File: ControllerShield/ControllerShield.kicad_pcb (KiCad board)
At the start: 2 copper layers, 68.6 x 53.5 mm, 30 parts, among them J1 Power, J2 Digital/PWM, J3 Analog, J4 Digital/PWM, J5 Conn_02x05_Odd_Even, J6 Debug Point, SW1 Small Switch TH, U1 COM-09032, U2 LIS3DHTR, U3 TLV75533PDBV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

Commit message: Close #13
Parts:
- moved D2 5.05 mm to (128.1, 91.7)
- moved D1 2.90 mm to (128.0, 134.7)
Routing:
- net Net-(D2-A): track 3.83 -> 8.00 mm, vias 0 -> 1
- net Net-(D1-A): track 30.9 -> 33.7 mm
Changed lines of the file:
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@@
   )
   (footprint "LED_THT:LED_D5.0mm" (layer "F.Cu")
-    (at 128 131.75)
+    (at 128.025 134.65)
     (descr "LED, diameter 5.0mm, 2 pins, http://cdn-reichelt.de/documents/datenblatt/A500/LL-504BC2E-009.pdf")
     (tags "LED diameter 5.0mm 2 pins")
@@
   )
   (footprint "LED_THT:LED_D5.0mm" (layer "F.Cu")
-    (at 128 96.75)
+    (at 128.075 91.7)
     (descr "LED, diameter 5.0mm, 2 pins, http://cdn-reichelt.de/documents/datenblatt/A500/LL-504BC2E-009.pdf")
     (tags "LED diameter 5.0mm 2 pins")
@@
     (property "ki_keywords" "LED diode")
     (attr through_hole)
-    (fp_text reference "D2" (at 1.27 -3.96) (layer "F.SilkS")
+    (fp_text reference "D2" (at -3.175 -0.5) (layer "F.SilkS")
         (effects (font (size 1 1) (thickness 0.15)))
     )
@@
   (segment (start 134 102.325) (end 134 103.75) (width 0.18) (layer "F.Cu") (net 5))
   (via (at 134 103.75) (size 0.5) (drill 0.3) (layers "F.Cu" "B.Cu") (net 5))
-  (segment (start 134 128.29) (end 130.54 131.75) (width 0.18) (layer "B.Cu") (net 5))
-  (segment (start 134 103.75) (end 134 128.29) (width 0.18) (layer "B.Cu") (net 5))
-  (segment (start 134 97.65) (end 133.1 96.75) (width 0.18) (layer "F.Cu") (net 6))
-  (segment (start 133.1 96.75) (end 130.54 96.75) (width 0.18) (layer "F.Cu") (net 6))
+  (segment (start 134 131.215) (end 130.565 134.65) (width 0.18) (layer "B.Cu") (net 5))
+  (segment (start 134 103.75) (end 134 131.215) (width 0.18) (layer "B.Cu") (net 5))
+  (segment (start 134 97.65) (end 132.9 97.65) (width 0.2) (layer "F.Cu") (net 6))
+  (segment (start 132.9 97.65) (end 132.6 97.35) (width 0.2) (layer "F.Cu") (net 6))
+  (via (at 132.6 97.35) (size 0.5) (drill 0.3) (layers "F.Cu" "B.Cu") (net 6))
+  (segment (start 132.6 97.35) (end 132.6 93.685) (width 0.2) (layer "B.Cu") (net 6))
+  (segment (start 132.6 93.685) (end 130.615 91.7) (width 0.2) (layer "B.Cu") (net 6))
   (segment (start 136.525 110.988) (end 136.6 111.063) (width 0.18) (layer "F.Cu") (net 10))
   (segment (start 136.525 109.75) (end 136.525 110.988) (width 0.18) (layer "F.Cu") (net 10))
@@
   (segment (start 140.746 96.504) (end 140.746 90.395) (width 0.127) (layer "B.Cu") (net 10))
   (segment (start 127.21 117.54) (end 124.71 117.54) (width 1.27) (layer "F.Cu") (net 11))
-  (segment (start 150.906 90.395) (end 148.301 93) (width 0.18) (layer "F.Cu") (net 12))
-  (segment (start 148.301 93) (end 124.25 93) (width 0.18) (layer "F.Cu") (net 12))
+  (segment (start 147.951 93.35) (end 124.6 93.35) (width 0.18) (layer "F.Cu") (net 12))
+  (segment (start 124.6 93.35) (end 124.25 93) (width 0.18) (layer "F.Cu") (net 12))
+  (segment (start 150.906 90.395) (end 147.951 93.35) (width 0.18) (layer "F.Cu") (net 12))
   (via (at 124.25 93) (size 0.5) (drill 0.3) (layers "F.Cu" "B.Cu") (net 12))
   (segment (start 124.25 112.04) (end 127.21 115) (width 0.18) (layer "B.Cu") (net 12))
   (segment (start 124.25 93) (end 124.25 112.04) (width 0.18) (layer "B.Cu") (net 12))
-  (segment (start 150.341 93.5) (end 125.5 93.5) (width 0.18) (layer "F.Cu") (net 17))
-  (segment (start 125.5 93.5) (end 125 94) (width 0.18) (layer "F.Cu") (net 17))
-  (segment (start 153.446 90.395) (end 150.341 93.5) (width 0.18) (layer "F.Cu") (net 17))
+  (segment (start 125.2 93.8) (end 125 94) (width 0.18) (layer "F.Cu") (net 17))
+  (segment (start 150.041 93.8) (end 125.2 93.8) (width 0.18) (layer "F.Cu") (net 17))
+  (segment (start 153.446 90.395) (end 150.041 93.8) (width 0.18) (layer "F.Cu") (net 17))
   (via (at 125 94) (size 0.5) (drill 0.3) (layers "F.Cu" "B.Cu") (net 17))
   (segment (start 125 111.862204) (end 125 94) (width 0.18) (layer "B.Cu") (net 17))
@@
   (segment (start 141.25 92.431) (end 143.286 90.395) (width 0.127) (layer "B.Cu") (net 28))
   (segment (start 140.75 100.75) (end 140.5 100.5) (width 0.18) (layer "B.Cu") (net 28))
-  (segment (start 158.526 90.395) (end 154.921 94) (width 0.18) (layer "F.Cu") (net 34))
-  (segment (start 126.25 94) (end 125.75 94.5) (width 0.18) (layer "F.Cu") (net 34))
-  (segment (start 154.921 94) (end 126.25 94) (width 0.18) (layer "F.Cu") (net 34))
+  (segment (start 126 94.25) (end 125.75 94.5) (width 0.18) (layer "F.Cu") (net 34))
+  (segment (start 154.671 94.25) (end 126 94.25) (width 0.18) (layer "F.Cu") (net 34))
+  (segment (start 158.526 90.395) (end 154.671 94.25) (width 0.18) (layer "F.Cu") (net 34))
   (via (at 125.75 94.5) (size 0.5) (drill 0.3) (layers "F.Cu" "B.Cu") (net 34))
   (segment (start 125.5 94.75) (end 125.5 110.49) (width 0.18) (layer "B.Cu") (net 34))
@@
   (segment (start 128.61 111.06) (end 129.75 109.92) (width 0.18) (layer "B.Cu") (net 34))
   (segment (start 126.07 111.06) (end 128.61 111.06) (width 0.18) (layer "B.Cu") (net 34))
-  (segment (start 127.0395 94.4605) (end 126.25 95.25) (width 0.18) (layer "F.Cu") (net 39))
-  (segment (start 157.0005 94.4605) (end 127.0395 94.4605) (width 0.18) (layer "F.Cu") (net 39))
-  (segment (start 161.066 90.395) (end 157.0005 94.4605) (width 0.18) (layer "F.Cu") (net 39))
+  (segment (start 161.066 90.395) (end 156.811 94.65) (width 0.18) (layer "F.Cu") (net 39))
+  (segment (start 126.85 94.65) (end 126.25 95.25) (width 0.18) (layer "F.Cu") (net 39))
+  (segment (start 156.811 94.65) (end 126.85 94.65) (width 0.18) (layer "F.Cu") (net 39))
   (via (at 126.25 95.25) (size 0.5) (drill 0.3) (layers "F.Cu" "B.Cu") (net 39))
   (segment (start 126.25 95.25) (end 126.25 108.75) (width 0.18) (layer "B.Cu") (net 39))

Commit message: update qr code and legend
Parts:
- removed the G*** at (140.2, 125.8)
- added G***: LOGO, QRCodes:v0.9, F.Cu at (137.8, 125.0)
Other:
- board text added: "Maze Controller V0.9 Copyright 2023 Tad Truex Dartmouth College"

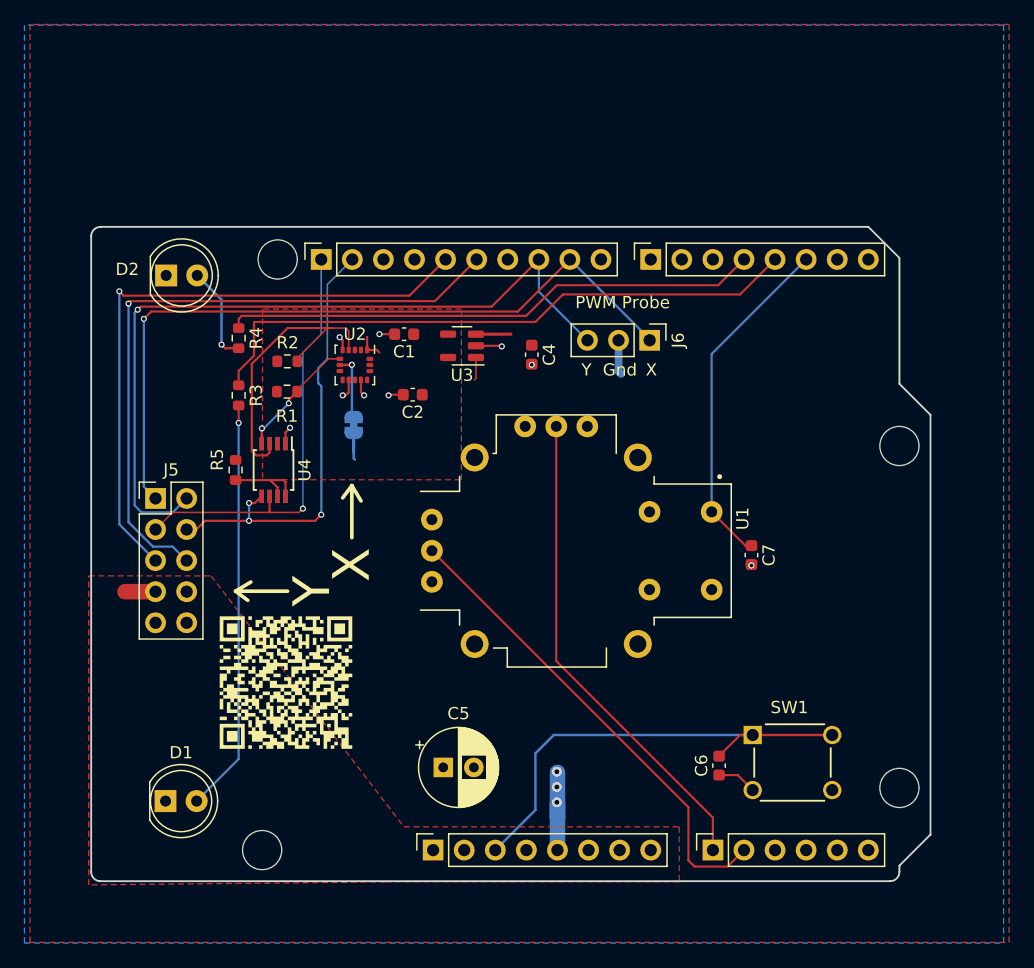
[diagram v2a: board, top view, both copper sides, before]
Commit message: Add a second switch to the controller board.
Generate V0.9 gerbers with QRCode.
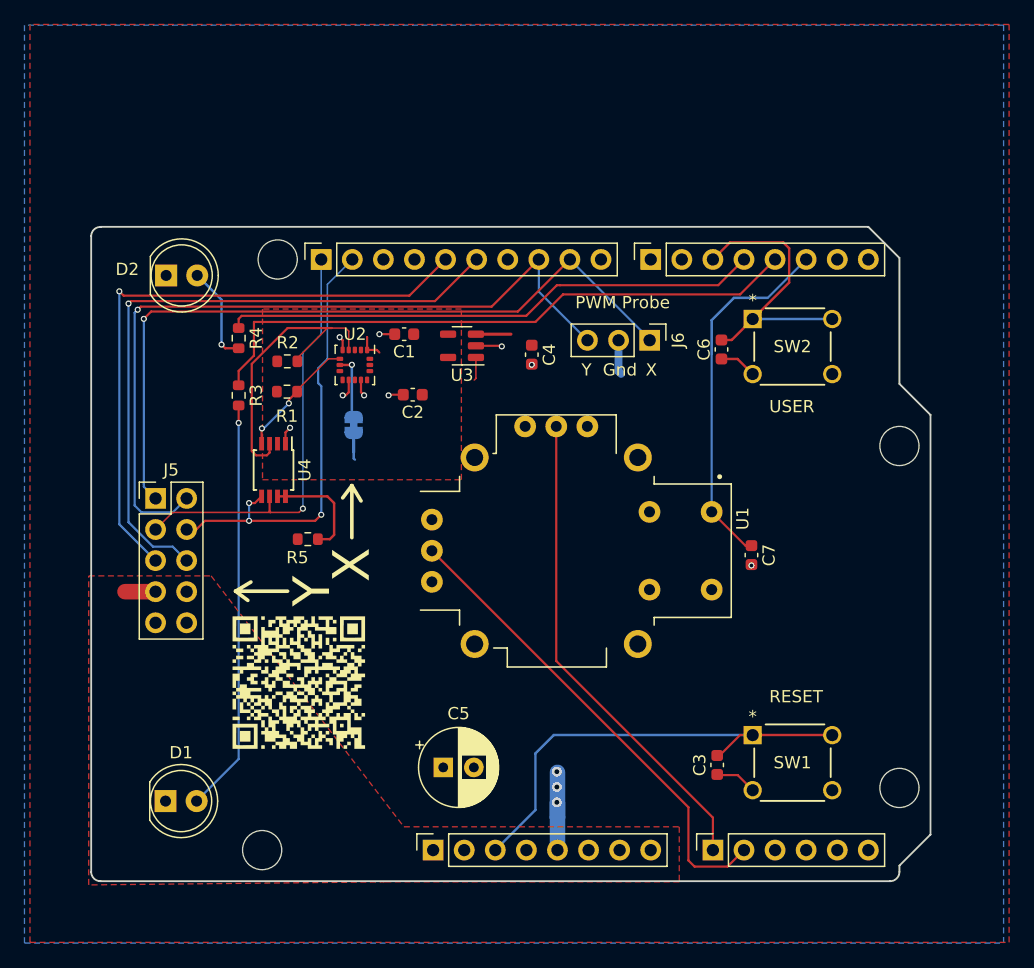
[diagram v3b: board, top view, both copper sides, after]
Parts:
- added C3: 0.1uF, Capacitor_SMD:C_0603_1608Metric, F.Cu at (173.1, 131.7)
- added SW2: Small Switch TH, Footprints:SW4_1825910-B_TEC, F.Cu at (182.5, 99.8)
- moved C6 34.0 mm to (173.4, 97.8)
- moved R5 8.17 mm to (139.7, 113.2), turned to 0 degrees
- moved G*** 1.05 mm to (138.9, 125.0)
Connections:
- C6 pad 2: /RSTn -> /ExtraBtn
- J4 pad 3: /*5 -> /ExtraBtn
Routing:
- net /ExtraBtn: track 0.00 -> 23.8 mm
- net GND: track 20.1 -> 23.1 mm
- net Net-(U4-EN): track 6.88 -> 8.92 mm
- net /GameBtn: track 28.2 -> 29.8 mm
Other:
- board text added: "RESET"
- board text added: "USER"

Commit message: Update controller shield to match the new driver.
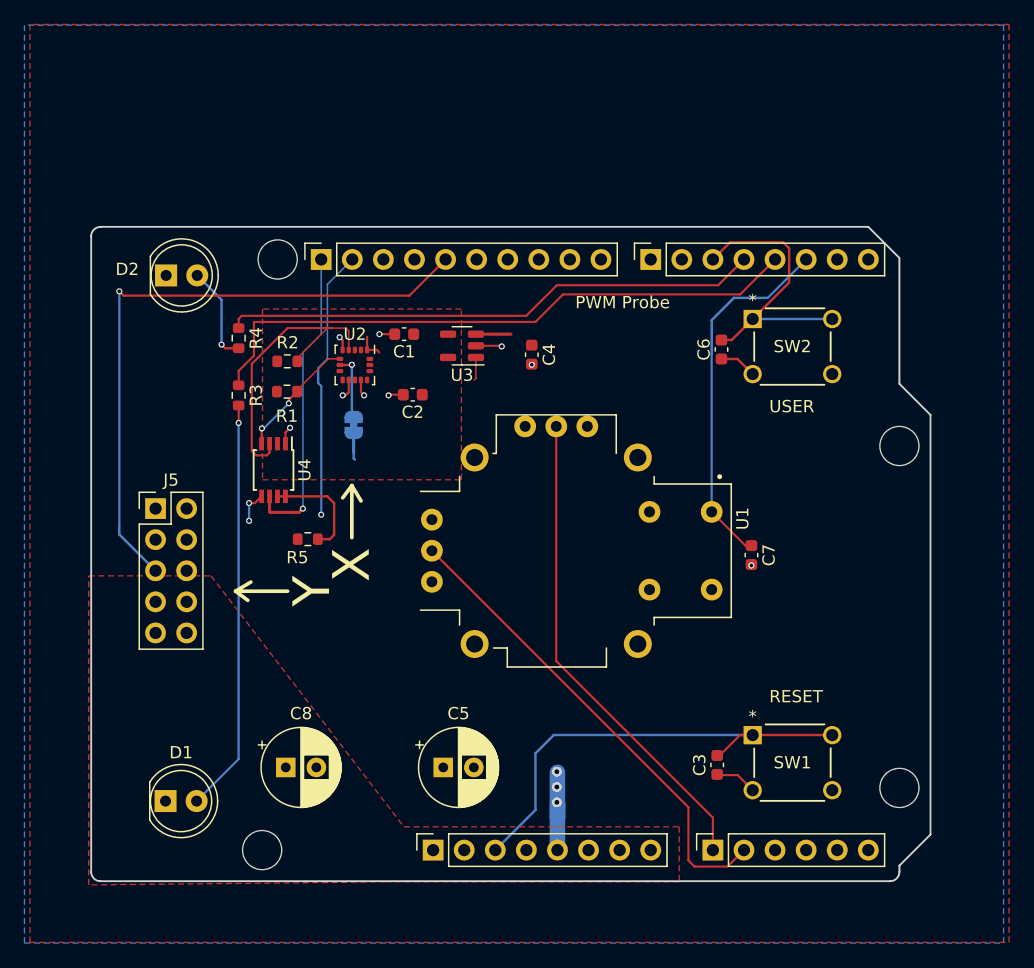
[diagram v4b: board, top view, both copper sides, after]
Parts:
- removed G***: LOGO, QRCodes:v0.9
- removed J6: Debug Point, Connector_PinHeader_2.54mm:PinHeader_1x03_P2.54mm_Vertical
- added C8: 10uF, Capacitor_THT:CP_Radial_D6.3mm_P2.50mm, F.Cu at (137.8, 131.9)
- moved J5 0.83 mm to (127.2, 110.8)
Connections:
- net /8 renamed /DirX
- J2 pad 7: /*11 -> /StepY
- J2 pad 8: /Y -> /DirY
- J2 pad 9: /X -> /StepX
- J5 pad 1: /X -> /SCL
- J5 pad 10: unconnected-(J5-Pin_10-Pad10) -> GND
- J5 pad 2: /Y -> /SCL
- J5 pad 7: /Vsys -> /StepY
- J5 pad 8: unconnected-(J5-Pin_8-Pad8) -> /DirY
- J5 pad 9: GND -> /Vsys
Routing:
- net /Y: track 63.8 -> 0.00 mm, vias 1 -> 0
- net /X: track 61.2 -> 0.00 mm, vias 1 -> 0
- net /D1: track 53.9 -> 0.00 mm, vias 1 -> 0
- net /SDA: track 36.3 -> 24.8 mm
- net /SCL: track 35.1 -> 25.1 mm
- net GND: track 23.1 -> 20.3 mm
- net /Vsys: track 2.50 -> 0.00 mm
- net /D0: track 51.3 -> 52.1 mm
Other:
- board text removed: "Gnd"

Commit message: Gerbers for both board V1.0
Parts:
- added G***: LOGO, QRCodes:v1.0, B.Cu at (139.8, 115.5)
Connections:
- J5 pad 1: /SCL -> /StepX
- J5 pad 2: /SCL -> /DirX
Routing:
- net /StepY: track 0.00 -> 57.8 mm, vias 0 -> 1
- net /DirY: track 0.00 -> 53.0 mm, vias 0 -> 1
- net /DirX: track 0.00 -> 51.2 mm, vias 0 -> 1
- net /StepX: track 0.00 -> 51.1 mm, vias 0 -> 1
- net /D1: track 0.00 -> 47.6 mm, vias 0 -> 1
- net /SCL: track 25.1 -> 40.9 mm, vias 1 -> 2
- net /SDA: track 24.8 -> 35.6 mm, vias 3 -> 1
- net /D0: track 52.1 -> 50.1 mm
- net /Red: track 50.4 -> 48.8 mm
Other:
- board text added: "Maze Controller V1.0 Copyright 2024 Tad Truex Dartmouth College"
- board text removed: "Maze Controller V0.9 Copyright 2023 Tad Truex Dartmouth College"
